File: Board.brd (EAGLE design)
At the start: 77.1 x 41.9 mm, 24 parts

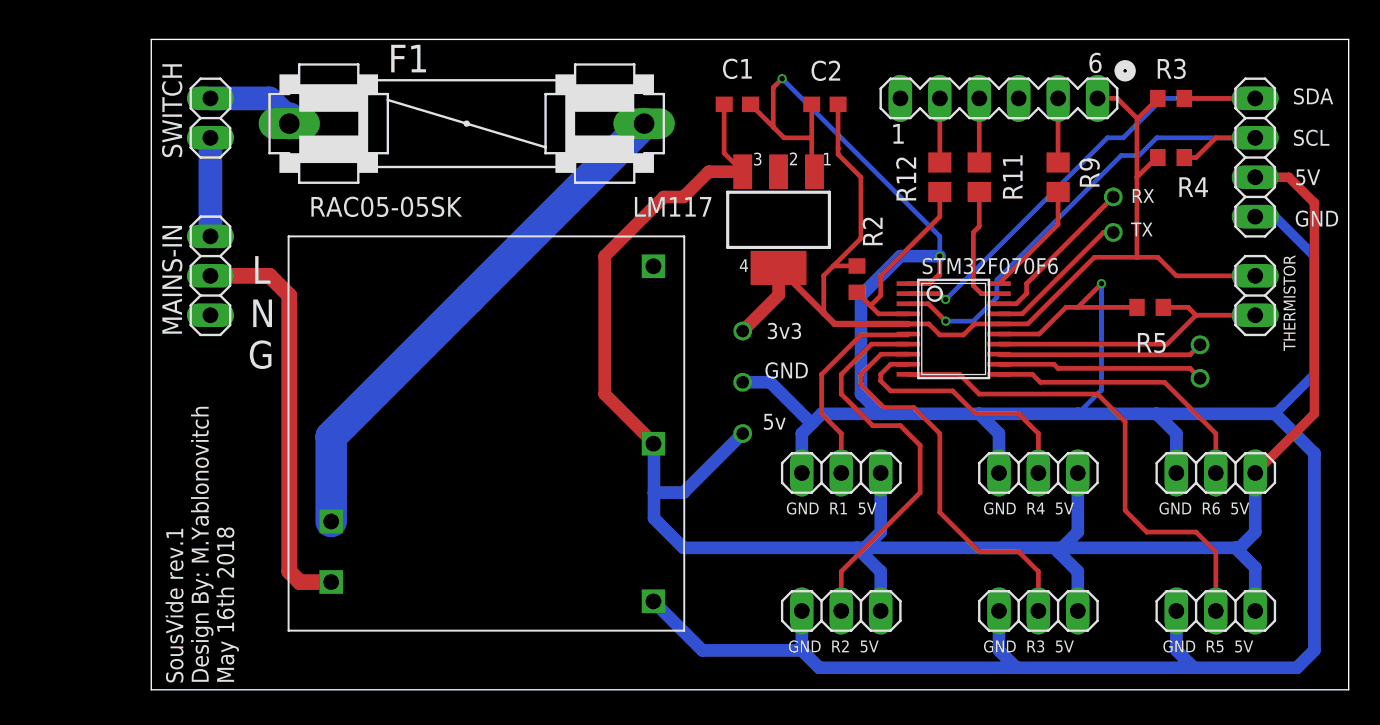
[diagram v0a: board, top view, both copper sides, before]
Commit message: premilinary rev 2, fixed Ac/DC footprint, removed on-board switch and added mains outputs
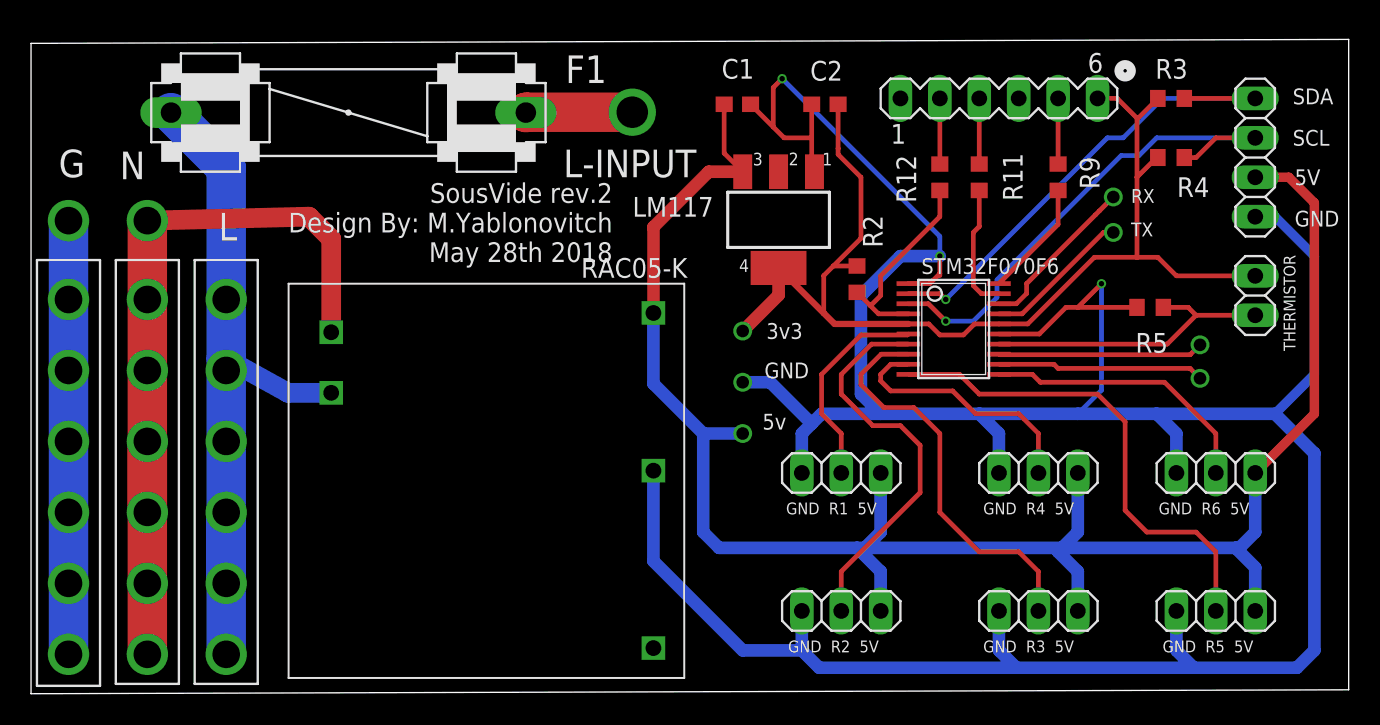
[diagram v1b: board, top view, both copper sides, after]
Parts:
- removed MAINS-IN: (no value), pinhead:1X03
- removed RAC05-05SK: AC/DC-CONVERTER, SousVide Library:AC/DC-CONVERTER
- removed SWITCH: (no value), pinhead:1X02
- added RAC05-K: AC/DC-CONVERTER, SousVide Library:AC/DC-CONVERTER
- R11, R12, R9: device rcl:R0805 -> rcl:R0603
- moved F1 7.65 mm to (12.7, 109.6), turned to 180 degrees
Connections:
- removed net N$7: MAINS-IN.3, SWITCH.1
- removed net PGND: MAINS-IN.1
- net +5V: now also RAC05-K.+5V; no longer RAC05-05SK.P$4
- net PE: now also RAC05-K.GND; no longer RAC05-05SK.P$5
- net VAC(L): now also RAC05-K.L; no longer RAC05-05SK.P$1
- net VAC(L)-INPUT: no longer SWITCH.2
- net VAC(N): now also RAC05-K.N; no longer MAINS-IN.2, RAC05-05SK.P$2
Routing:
- net VAC(G): track 0.00 -> 27.9 mm, vias 0 -> 7
- net VAC(N): track 26.4 -> 51.0 mm, vias 0 -> 7
- net VAC(L): track 34.0 -> 48.3 mm, vias 0 -> 6
- net +5V: track 133.2 -> 123.7 mm
- net PE: track 203.5 -> 210.4 mm
- net N$7: track 6.35 -> 0.00 mm
- net VAC(L)-INPUT: track 5.96 -> 6.87 mm, vias 0 -> 1
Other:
- board size 77.1 x 41.9 mm -> 84.9 x 42.2 mm
- board text added: "L-INPUT"
- board text added: "SousVide rev.2 Design By: M.Yablonovitch May 28th 2018"
- board text removed: "SousVide rev.1 Design By: M.Yablonovitch May 16th 2018"

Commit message: added DC power LEDs
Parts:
- added D1, D2: (no value), SparkFun-LED:LED-0603
- added R1, R6: 250, rcl:R0603
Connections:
- removed net PE: C1.2, C2.2, JP1.4, JP2.3, JP4.3, JP5.3, JP6.3, JP7.3, JP8.3, LM117.1, R5.2, RAC05-K.GND, STM32F070F6.1, STM32F070F6.15
- new net N$1: D1.C, R1.1
- new net N$2: D2.C, R6.1
- net +3V3: now also D1.A
- net +5V: now also D2.A
- net GND: now also C1.2, C2.2, JP1.4, JP2.3, JP4.3, JP5.3, JP6.3, JP7.3, JP8.3, LM117.1, R1.2, R5.2, R6.2, RAC05-K.GND, STM32F070F6.1, STM32F070F6.15
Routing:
- net GND: track 0.00 -> 231.9 mm, vias 0 -> 4
- net PE: track 210.4 -> 0.00 mm, vias 4 -> 0
- net +3V3: track 72.4 -> 83.4 mm
- net +5V: track 123.7 -> 127.4 mm
- net N$1: track 0.00 -> 2.59 mm
- net N$2: track 0.00 -> 2.33 mm
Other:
- board text added: "3.3v"
